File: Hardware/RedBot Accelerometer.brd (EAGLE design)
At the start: 14 x 17.8 mm, 20 parts, among them U1 MMA8452QMMA8452Q-1:1, U2 MIC5205-3.3V, U3 PCA9306

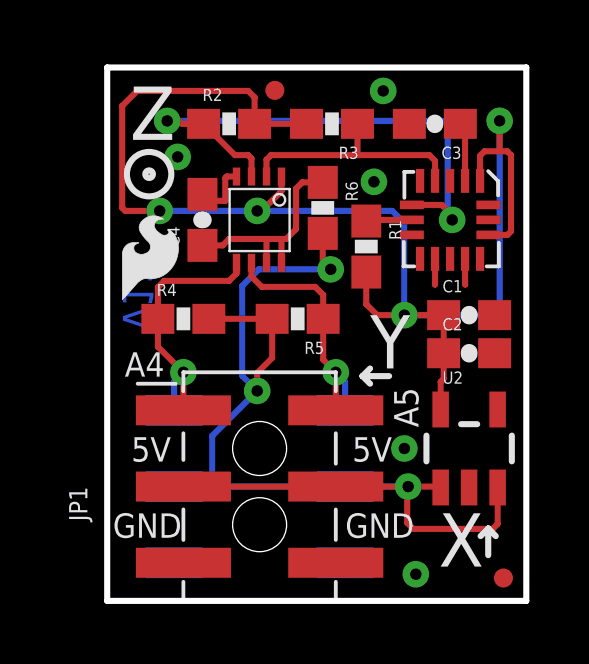
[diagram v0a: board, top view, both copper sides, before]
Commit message: changed fids from micro to regular
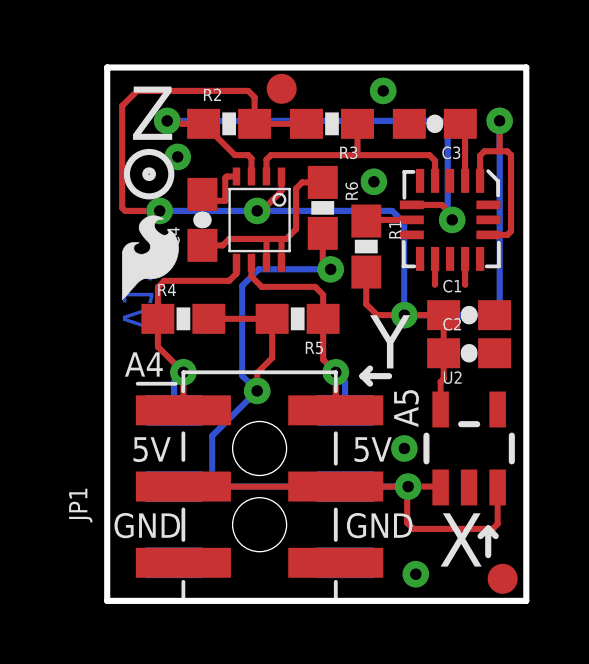
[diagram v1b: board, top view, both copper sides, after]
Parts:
- removed FID2: FIDUCIALUFIDUCIAL, SparkFun-Aesthetics:MICRO-FIDUCIAL
- added FID3: FIDUCIAL1X2, SparkFun-Aesthetics:FIDUCIAL-1X2
- FID1: value FIDUCIALUFIDUCIAL -> FIDUCIAL1X2; device SparkFun-Aesthetics:MICRO-FIDUCIAL -> SparkFun-Aesthetics:FIDUCIAL-1X2
- moved FID1 17.9 mm to (5.82, 17.1)
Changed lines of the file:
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@@
 <setting verticaltext="up"/>
 </settings>
-<grid distance="0.05" unitdist="inch" unit="inch" style="lines" multiple="1" display="yes" altdistance="0.005" altunitdist="inch" altunit="inch"/>
+<grid distance="0.01" unitdist="inch" unit="inch" style="lines" multiple="1" display="yes" altdistance="0.001" altunitdist="inch" altunit="inch"/>
 <layers>
 <layer number="1" name="Top" color="4" fill="1" visible="yes" active="yes"/>
-<layer number="2" name="Route2" color="1" fill="3" visible="no" active="yes"/>
-<layer number="15" name="Route15" color="4" fill="6" visible="no" active="yes"/>
+<layer number="2" name="Route2" color="1" fill="3" visible="yes" active="yes"/>
+<layer number="15" name="Route15" color="4" fill="6" visible="yes" active="yes"/>
 <layer number="16" name="Bottom" color="1" fill="1" visible="yes" active="yes"/>
 <layer number="17" name="Pads" color="2" fill="1" visible="yes" active="yes"/>
 <layer number="18" name="Vias" color="2" fill="1" visible="yes" active="yes"/>
 <layer number="19" name="Unrouted" color="6" fill="1" visible="yes" active="yes"/>
-<layer number="20" name="Dimension" color="15" fill="1" visible="yes" active="yes"/>
-<layer number="21" name="tPlace" color="16" fill="1" visible="yes" active="yes"/>
-<layer number="22" name="bPlace" color="14" fill="1" visible="yes" active="yes"/>
+<layer number="20" name="Dimension" color="6" fill="1" visible="yes" active="yes"/>
+<layer number="21" name="tPlace" color="6" fill="1" visible="yes" active="yes"/>
+<layer number="22" name="bPlace" color="6" fill="1" visible="yes" active="yes"/>
 <layer number="23" name="tOrigins" color="15" fill="1" visible="yes" active="yes"/>
 <layer number="24" name="bOrigins" color="15" fill="1" visible="yes" active="yes"/>
-<layer number="25" name="tNames" color="7" fill="1" visible="no" active="yes"/>
-<layer number="26" name="bNames" color="7" fill="1" visible="no" active="yes"/>
-<layer number="27" name="tValues" color="7" fill="1" visible="no" active="yes"/>
-<layer number="28" name="bValues" color="7" fill="1" visible="no" active="yes"/>
-<layer number="29" name="tStop" color="7" fill="3" visible="no" active="yes"/>
-<layer number="30" name="bStop" color="7" fill="6" visible="no" active="yes"/>
-<layer number="31" name="tCream" color="7" fill="4" visible="no" active="yes"/>
-<layer number="32" name="bCream" color="7" fill="5" visible="no" active="yes"/>
-<layer number="39" name="tKeepout" color="4" fill="11" visible="no" active="yes"/>
-<layer number="40" name="bKeepout" color="1" fill="11" visible="no" active="yes"/>
-<layer number="41" name="tRestrict" color="4" fill="10" visible="no" active="yes"/>
-<layer number="42" name="bRestrict" color="1" fill="10" visible="no" active="yes"/>
-<layer number="43" name="vRestrict" color="2" fill="10" visible="no" active="yes"/>
-<layer number="44" name="Drills" color="7" fill="1" visible="no" active="yes"/>
+<layer number="25" name="tNames" color="7" fill="1" visible="yes" active="yes"/>
+<layer number="26" name="bNames" color="7" fill="1" visible="yes" active="yes"/>
+<layer number="27" name="tValues" color="7" fill="1" visible="yes" active="yes"/>
+<layer number="28" name="bValues" color="7" fill="1" visible="yes" active="yes"/>
+<layer number="29" name="tStop" color="7" fill="3" visible="yes" active="yes"/>
+<layer number="30" name="bStop" color="7" fill="6" visible="yes" active="yes"/>
+<layer number="31" name="tCream" color="7" fill="4" visible="yes" active="yes"/>
+<layer number="32" name="bCream" color="7" fill="5" visible="yes" active="yes"/>
+<layer number="39" name="tKeepout" color="4" fill="11" visible="yes" active="yes"/>
+<layer number="40" name="bKeepout" color="1" fill="11" visible="yes" active="yes"/>
+<layer number="41" name="tRestrict" color="4" fill="10" visible="yes" active="yes"/>
+<layer number="42" name="bRestrict" color="1" fill="10" visible="yes" active="yes"/>
+<layer number="43" name="vRestrict" color="2" fill="10" visible="yes" active="yes"/>
+<layer number="44" name="Drills" color="7" fill="1" visible="yes" active="yes"/>
 <layer number="45" name="Holes" color="7" fill="1" visible="yes" active="yes"/>
-<layer number="46" name="Milling" color="3" fill="1" visible="no" active="yes"/>
+<layer number="46" name="Milling" color="3" fill="1" visible="yes" active="yes"/>
 <layer number="51" name="tDocu" color="6" fill="1" visible="yes" active="yes"/>
-<layer number="52" name="bDocu" color="7" fill="1" visible="no" active="yes"/>
+<layer number="52" name="bDocu" color="7" fill="1" visible="yes" active="yes"/>
 <layer number="3" name="Route3" color="4" fill="3" visible="no" active="no"/>
 <layer number="4" name="Route4" color="1" fill="4" visible="no" active="no"/>
@@
 <layer number="108" name="tplace-old" color="10" fill="1" visible="no" active="no"/>
 <layer number="109" name="ref-old" color="11" fill="1" visible="no" active="no"/>
-<layer number="110" name="fp0" color="7" fill="1" visible="no" active="yes"/>
-<layer number="111" name="LPC17xx" color="7" fill="1" visible="no" active="yes"/>
-<layer number="112" name="tSilk" color="7" fill="1" visible="no" active="yes"/>
-<layer number="113" name="IDFDebug" color="7" fill="1" visible="no" active="yes"/>
+<layer number="110" name="fp0" color="7" fill="1" visible="yes" active="yes"/>
+<layer number="111" name="LPC17xx" color="7" fill="1" visible="yes" active="yes"/>
+<layer number="112" name="tSilk" color="7" fill="1" visible="yes" active="yes"/>
+<layer number="113" name="IDFDebug" color="7" fill="1" visible="yes" active="yes"/>
 <layer number="116" name="Patch_BOT" color="9" fill="4" visible="no" active="no"/>
 <layer number="121" name="_tsilk" color="7" fill="1" visible="no" active="no"/>
 <layer number="122" name="_bsilk" color="7" fill="1" visible="no" active="no"/>
-<layer number="123" name="tTestmark" color="7" fill="1" visible="no" active="yes"/>
-<layer number="124" name="bTestmark" color="7" fill="1" visible="no" active="yes"/>
+<layer number="123" name="tTestmark" color="7" fill="1" visible="yes" active="yes"/>
+<layer number="124" name="bTestmark" color="7" fill="1" visible="yes" active="yes"/>
 <layer number="125" name="_tNames" color="7" fill="1" visible="no" active="no"/>
-<layer number="126" name="_bNames" color="7" fill="1" visible="no" active="yes"/>
-<layer number="127" name="_tValues" color="7" fill="1" visible="no" active="yes"/>
-<layer number="128" name="_bValues" color="7" fill="1" visible="no" active="yes"/>
-<layer number="131" name="tAdjust" color="7" fill="1" visible="no" active="yes"/>
-<layer number="132" name="bAdjust" color="7" fill="1" visible="no" active="yes"/>
+<layer number="126" name="_bNames" color="7" fill="1" visible="yes" active="yes"/>
+<layer number="127" name="_tValues" color="7" fill="1" visible="yes" active="yes"/>
+<layer number="128" name="_bValues" color="7" fill="1" visible="yes" active="yes"/>
+<layer number="131" name="tAdjust" color="7" fill="1" visible="yes" active="yes"/>
+<layer number="132" name="bAdjust" color="7" fill="1" visible="yes" active="yes"/>
 <layer number="144" name="Drill_legend" color="7" fill="1" visible="no" active="no"/>
-<layer number="150" name="Notes" color="7" fill="1" visible="no" active="yes"/>
+<layer number="150" name="Notes" color="7" fill="1" visible="yes" active="yes"/>
 <layer number="151" name="HeatSink" color="7" fill="1" visible="no" active="no"/>
-<layer number="152" name="_bDocu" color="7" fill="1" visible="no" active="yes"/>
-<layer number="153" name="FabDoc1" color="7" fill="1" visible="no" active="yes"/>
-<layer number="154" name="FabDoc2" color="7" fill="1" visible="no" active="yes"/>
-<layer number="155" name="FabDoc3" color="7" fill="1" visible="no" active="yes"/>
+<layer number="152" name="_bDocu" color="7" fill="1" visible="yes" active="yes"/>
+<layer number="153" name="FabDoc1" color="7" fill="1" visible="yes" active="yes"/>
+<layer number="154" name="FabDoc2" color="7" fill="1" visible="yes" active="yes"/>
+<layer number="155" name="FabDoc3" color="7" fill="1" visible="yes" active="yes"/>
 <layer number="199" name="Contour" color="7" fill="1" visible="no" active="no"/>
 <layer number="200" name="200bmp" color="1" fill="10" visible="no" active="no"/>
@@
 <layer number="223" name="223bmp" color="24" fill="1" visible="no" active="no"/>
 <layer number="224" name="224bmp" color="25" fill="1" visible="no" active="no"/>
-<layer number="248" name="Housing" color="7" fill="1" visible="no" active="yes"/>
-<layer number="249" name="Edge" color="7" fill="1" visible="no" active="yes"/>
+<layer number="248" name="Housing" color="7" fill="1" visible="yes" active="yes"/>
+<layer number="249" name="Edge" color="7" fill="1" visible="yes" active="yes"/>
 <layer number="250" name="Descript" color="3" fill="1" visible="no" active="no"/>
 <layer number="251" name="SMDround" color="12" fill="11" visible="no" active="no"/>
@@
 <attribute name="PROD_ID" value="CONN-11290" x="5.08" y="3.81" size="1.778" layer="28" font="vector" ratio="15" rot="MR270" display="off"/>
 </element>
-<element name="FID1" library="SparkFun-Aesthetics" package="MICRO-FIDUCIAL" value="FIDUCIALUFIDUCIAL" x="13.208" y="0.762"/>
-<element name="FID2" library="SparkFun-Aesthetics" package="MICRO-FIDUCIAL" value="FIDUCIALUFIDUCIAL" x="5.588" y="17.018"/>
+<element name="FID3" library="SparkFun-Aesthetics" package="FIDUCIAL-1X2" value="FIDUCIAL1X2" x="13.1826" y="0.7366"/>
+<element name="FID1" library="SparkFun-Aesthetics" package="FIDUCIAL-1X2" value="FIDUCIAL1X2" x="5.8166" y="17.0688"/>
 </elements>
 <signals>

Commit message: pushing v14
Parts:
- removed C4: 0.1uF, SparkFun-Capacitors:0603-CAP
- removed R2, R3, R4, R5: 1k, SparkFun-Resistors:0603-RES
- removed R6: 200k, SparkFun-Resistors:0603-RES
- removed U3: PCA9306, SparkFun-DigitalIC:PCA9306DC-1:1
- added I2C: JUMPER-SMT_3_2-NC_TRACE_SILK, SparkFun-Jumpers:SMT-JUMPER_3_2-NC_TRACE_SILK
- added LOGO3: LOGO-SFESK, SparkFun-Aesthetics:SFE-LOGO-FLAME
- added Q1, Q2: 220mA/50V/3.5Ω, SparkFun-DiscreteSemi:SOT23-3
- added R10, R7, R8, R9: 10k, SparkFun-Resistors:0603
- added U$1: (no value), buzzard_labels (17):X0
- added U$10: (no value), buzzard_labels (18):_SCL7
- added U$11, U$4, U$5, U$8: (no value), buzzard_labels (18):_5V1
- added U$12: (no value), buzzard_labels (17):##3
- added U$13: (no value), buzzard_labels (17):##4
- added U$14: (no value), buzzard_labels (17):Y1
- added U$15: (no value), buzzard_labels (17):Z2
- added U$16: (no value), buzzard_labels (18):REDBOT4
- added U$17: (no value), buzzard_labels (18):ACCELEROMETER5
- added U$19: (no value), SparkFun-Buzzard:I2C
- added U$2: (no value), buzzard_labels (18):A42
- added U$3: (no value), buzzard_labels (18):A53
- added U$6, U$7: (no value), buzzard_labels (18):GND0
- added U$9: (no value), buzzard_labels (18):SDA6
- moved FRAME1 22.2 mm to (-21.6, -7.62)
- moved LOGO1 14.2 mm to (10.9, 0.38)
- moved FID1 1.55 mm to (7.34, 16.8)
- moved FID3 0.36 mm to (12.9, 0.99)
- moved U2 0.25 mm to (12.1, 5.33)
- moved R1 0.20 mm to (8.43, 11.8)
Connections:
- removed net N$2: C4.1, R6.1, U3.7, U3.8
- removed net SCL1: R3.1, U1.4, U3.2
- removed net SDA1: R2.1, U1.6, U3.3
- new net LSCL: Q2.2, R9.1, U1.4
- new net LSDA: Q1.2, R8.1, U1.6
- new net N$3: I2C.3, R7.2
- new net N$4: I2C.1, R10.2
- net 3.3V: now also Q1.1, Q2.1, R8.2, R9.2; no longer R2.2, R3.2, U3.1
- net 5V: now also I2C.2; no longer R4.2, R5.2, R6.2
- net GND: no longer C4.2, U3.4
- net SCL: now also Q2.3, R10.1; no longer R5.1, U3.6
- net SDA: now also Q1.3, R7.1; no longer R4.1, U3.5
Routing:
- net SDA1: track 18.2 -> 0.00 mm, vias 2 -> 0
- net 3.3V: track 47.9 -> 36.5 mm
- net LSDA: track 0.00 -> 10.7 mm, vias 0 -> 2
- net LSCL: track 0.00 -> 10.5 mm
- net SCL1: track 8.04 -> 0.00 mm
- net N$2: track 7.29 -> 0.00 mm
- net N$3: track 0.00 -> 5.62 mm
- net SCL: track 8.53 -> 13.4 mm
- net 5V: track 38.7 -> 42.7 mm, vias 3 -> 1
- net N$4: track 0.00 -> 3.24 mm
- net SDA: track 9.02 -> 11.1 mm
- net GND: track 3.73 -> 1.72 mm, vias 5 -> 6
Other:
- board text added: "Revised by: Patrick Alberts, Andy England"
- board text added: "v14"
- board text removed: "5V"
- board text removed: "A4"
- board text removed: "A5"
- board text removed: "GND"
- board text removed: "RedBot Accelerometer Board"
- board text removed: "Revised by: Patrick Alberts"
- board text removed: "SCL"
- board text removed: "SDA"
- board text removed: "X"
- board text removed: "Y"
- board text removed: "Z"
- board text removed: "v12"

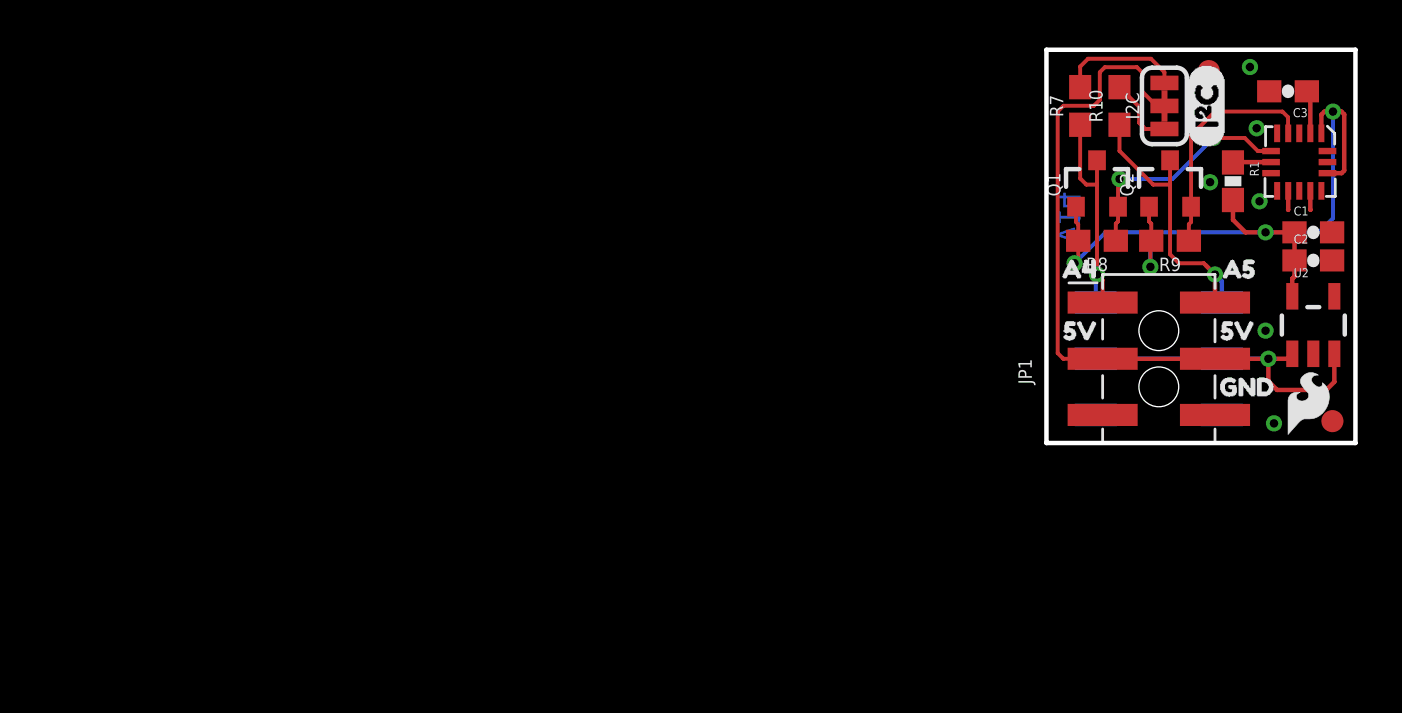
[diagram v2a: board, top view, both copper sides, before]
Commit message: updating old packages
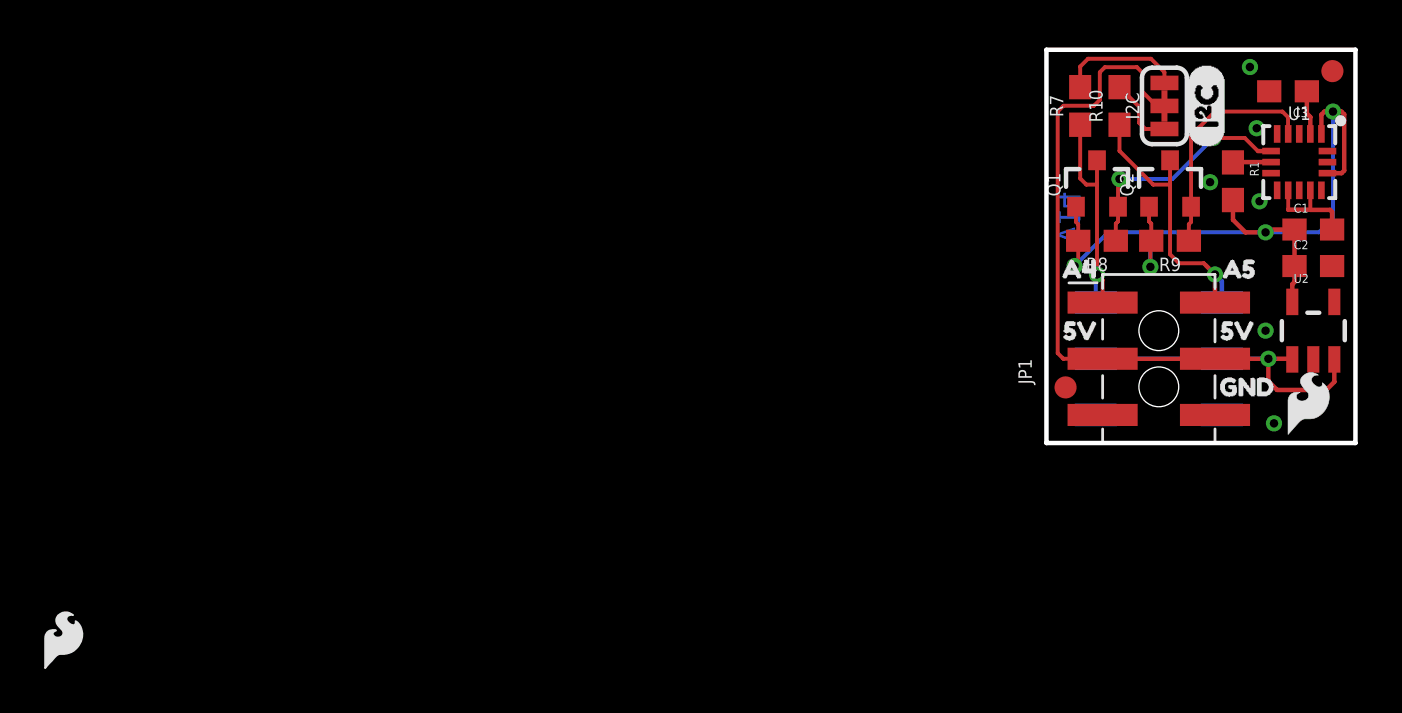
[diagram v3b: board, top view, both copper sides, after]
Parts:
- added LOGO4: SFE_LOGO_FLAME.1_INCH, SparkFun-Aesthetics:SFE_LOGO_FLAME_.1
- C1, C2, C3: device SparkFun-Capacitors:0603-CAP -> SparkFun-Capacitors:0603
- R1: device SparkFun-Resistors:0603-RES -> SparkFun-Resistors:0603
- U1: value MMA8452QMMA8452Q-1:1 -> MMA8452Q; device SparkFun-Sensors:MMA8452Q-1:1 -> SparkFun-Sensors:QFN-16
- moved FID3 12.2 mm to (0.86, 2.51)
- moved FID1 5.59 mm to (12.9, 16.8)
- moved C2 0.25 mm to (12.1, 8.00)
- moved U2 0.25 mm to (12.1, 5.08)
- moved C1 0.13 mm to (12.1, 9.65)
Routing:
- net GND: track 1.72 -> 4.59 mm
- net 3.3V: track 36.5 -> 37.2 mm

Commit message: post-review changes
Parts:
- removed LOGO1: LOGO-SFESK, SparkFun-Aesthetics:SFE-LOGO-FLAME
- moved LOGO4 57.2 mm to (11.8, 1.65)
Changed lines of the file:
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@@
 <attribute name="REV" value="" x="-21.59" y="-7.62" size="1.778" layer="27" display="off"/>
 </element>
-<element name="LOGO1" library="SparkFun-Aesthetics" package="SFE-LOGO-FLAME" value="LOGO-SFESK" x="10.922" y="0.381" smashed="yes"/>
 <element name="LOGO2" library="SparkFun-Aesthetics" package="OSHW-LOGO-S" value="OSHW-LOGOS" x="11.43" y="14.224" smashed="yes" rot="MR0"/>
 <element name="C1" library="SparkFun-Capacitors" package="0603" value="0.1uF" x="12.065" y="9.652" smashed="yes">
@@
 <element name="U$19" library="SparkFun-Buzzard" package="I2C" value="" x="7.239" y="13.335" smashed="yes" rot="R90"/>
 <element name="LOGO3" library="SparkFun-Aesthetics" package="SFE-LOGO-FLAME" value="LOGO-SFESK" x="3.048" y="13.081" smashed="yes" rot="MR0"/>
-<element name="LOGO4" library="SparkFun-Aesthetics" package="SFE_LOGO_FLAME_.1" value="SFE_LOGO_FLAME.1_INCH" x="-44.45" y="-8.89" smashed="yes"/>
+<element name="LOGO4" library="SparkFun-Aesthetics" package="SFE_LOGO_FLAME_.1" value="SFE_LOGO_FLAME.1_INCH" x="11.811" y="1.651" smashed="yes"/>
 <element name="U1" library="SparkFun-Sensors" package="QFN-16" value="MMA8452Q" x="11.43" y="12.7" smashed="yes" rot="R270">
 <attribute name="NAME" x="11.43" y="14.605" size="0.6096" layer="25" font="vector" ratio="20" align="bottom-center"/>

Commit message: panelizing
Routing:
- net SCL: track 13.4 -> 15.3 mm
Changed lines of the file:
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@@
 <contactref element="U1" pad="10"/>
 <wire x1="10.93" y1="11.425" x2="10.93" y2="10.549" width="0.1778" layer="1"/>
-<wire x1="10.93" y1="10.549" x2="10.922" y2="10.541" width="0.1778" layer="1"/>
 <wire x1="11.93" y1="11.425" x2="11.93" y2="10.549" width="0.1778" layer="1"/>
 <wire x1="10.93" y1="10.549" x2="11.93" y2="10.549" width="0.2032" layer="1"/>
@@
 <contactref element="JP1" pad="2"/>
 <contactref element="JP2" pad="1"/>
-<wire x1="7.62" y1="7.62" x2="7.2" y2="8.04" width="0.2032" layer="1"/>
-<wire x1="7.62" y1="7.62" x2="7.62" y2="6.35" width="0.2032" layer="1"/>
-<wire x1="7.93" y1="6.35" x2="7.93" y2="7.31" width="0.2032" layer="16"/>
-<wire x1="7.93" y1="7.31" x2="7.62" y2="7.62" width="0.2032" layer="16"/>
-<via x="7.62" y="7.62" extent="1-16" drill="0.381"/>
+<wire x1="7.62" y1="8.636" x2="7.62" y2="8.128" width="0.2032" layer="1"/>
+<wire x1="7.62" y1="8.128" x2="7.62" y2="6.35" width="0.2032" layer="1"/>
+<wire x1="7.93" y1="6.35" x2="7.93" y2="8.326" width="0.2032" layer="16"/>
+<wire x1="7.93" y1="8.326" x2="7.62" y2="8.636" width="0.2032" layer="16"/>
+<via x="7.62" y="8.636" extent="1-16" drill="0.381"/>
 <contactref element="Q2" pad="3"/>
 <contactref element="R10" pad="1"/>
-<wire x1="7.2" y1="8.04" x2="7.112" y2="8.128" width="0.1778" layer="1"/>
 <wire x1="5.588" y1="8.53090625" x2="5.99090625" y2="8.128" width="0.1778" layer="1"/>
-<wire x1="7.112" y1="8.128" x2="5.99090625" y2="8.128" width="0.1778" layer="1"/>
 <wire x1="5.588" y1="12.784" x2="5.588" y2="11.684" width="0.1778" layer="1"/>
 <wire x1="5.588" y1="11.684" x2="5.588" y2="8.53090625" width="0.1778" layer="1"/>
@@
 <wire x1="4.826" y1="11.684" x2="3.302" y2="13.208" width="0.1778" layer="1"/>
 <wire x1="3.302" y1="13.208" x2="3.302" y2="14.39" width="0.1778" layer="1"/>
+<wire x1="5.99090625" y1="8.128" x2="7.62" y2="8.128" width="0.1778" layer="1"/>
 </signal>
 <signal name="SDA">
